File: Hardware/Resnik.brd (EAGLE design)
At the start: 64.8 x 100 mm, 213 parts, among them IC1 ATMEGA644M, J1 CONN_82.54_SCREW, J3 CONN_42.54_SCREW, J4 CONN_82.54_SCREW, Q1 DMG3404, Q2 DMG3404, Q3 FDN360P, Q4 2N7002, Q5 FDN360P, Q6 DMG3404, Q7 2N7002, Q8 2N7002, U1 TLV61220DBV, U10 TPS22917DBV, U11 SN74AUP1G04YFP, U12 SN74AUP1G04YFP, U13 SN74AUP1G04YFP, U14 SN74AUP2G08DQE, U15 SN74AUP2G08DQE, U16 SN74AUP2G08DQE, U17 MIC2544MSOP, U18 MIC2544MSOP, U19 MIC2544MSOP, U2 TPS62822DLC, U20 MIC2544MSOP, U21 TPS22917DBV, U22 TPS22917DBV, U23 FT231X-Q, U24 SN74LVC1G3157DRL, U25 SN74AUP3G34DCU, U26 TXS0102DQM, U27 TXS0104RGY, U28 TCA9406DCU, U29 TXS0104RGY, U3 TPS61032RSA, U30 MCP4726A2SOT-23, U31 BME280, U32 ADS1115, U33 ADS1115, U34 INA211DCK, U35 INA210DCK, U36 TCA9406DCU, U37 TLV3691DCK, U38 TS5A21366RSE, U39 MIC94090C6, U40 SN74AHC1G86DCK, U41 MCP23018QFN, U42 TXS0104RGY, U5 BQ2980RUG, U6 TPS2105, U7 LTC4412S6, U8 TPL5111DDC, U9 TPS79733

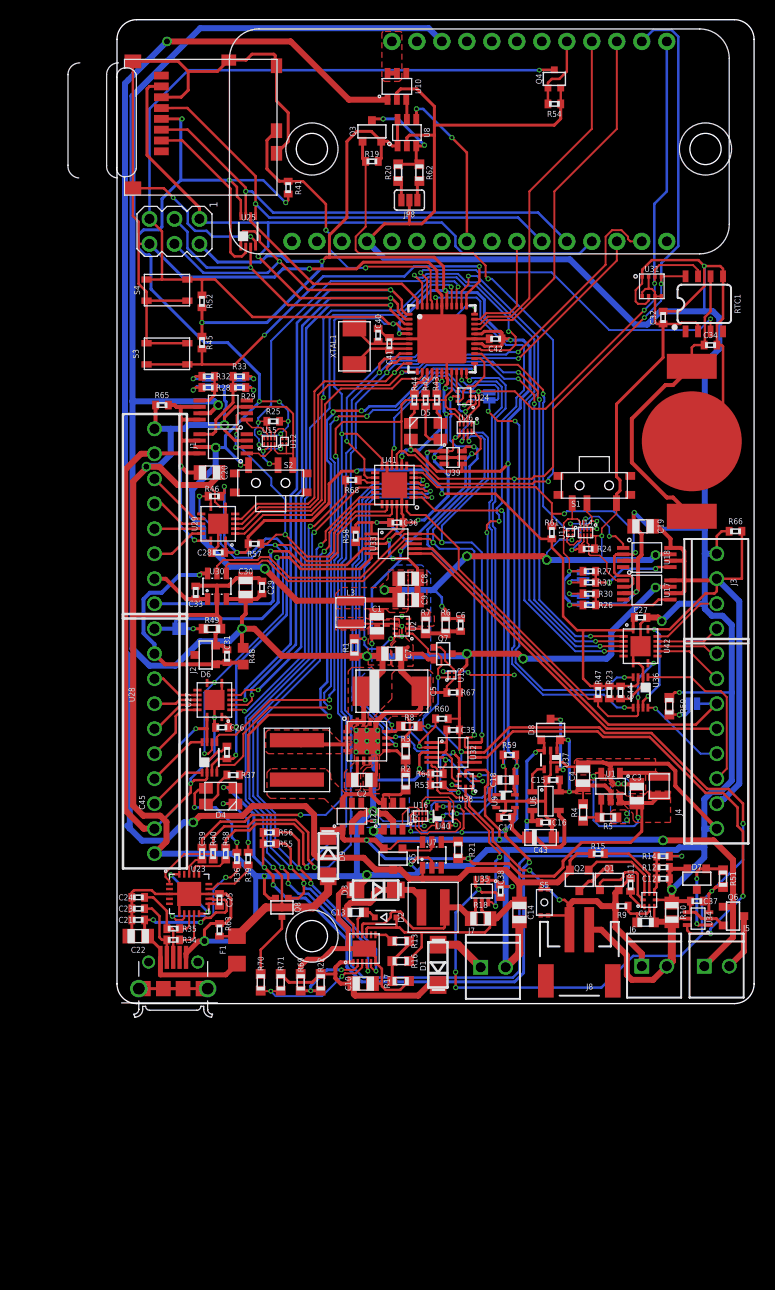
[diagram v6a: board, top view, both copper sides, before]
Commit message: Minor value changes, generated BoM for quote generation
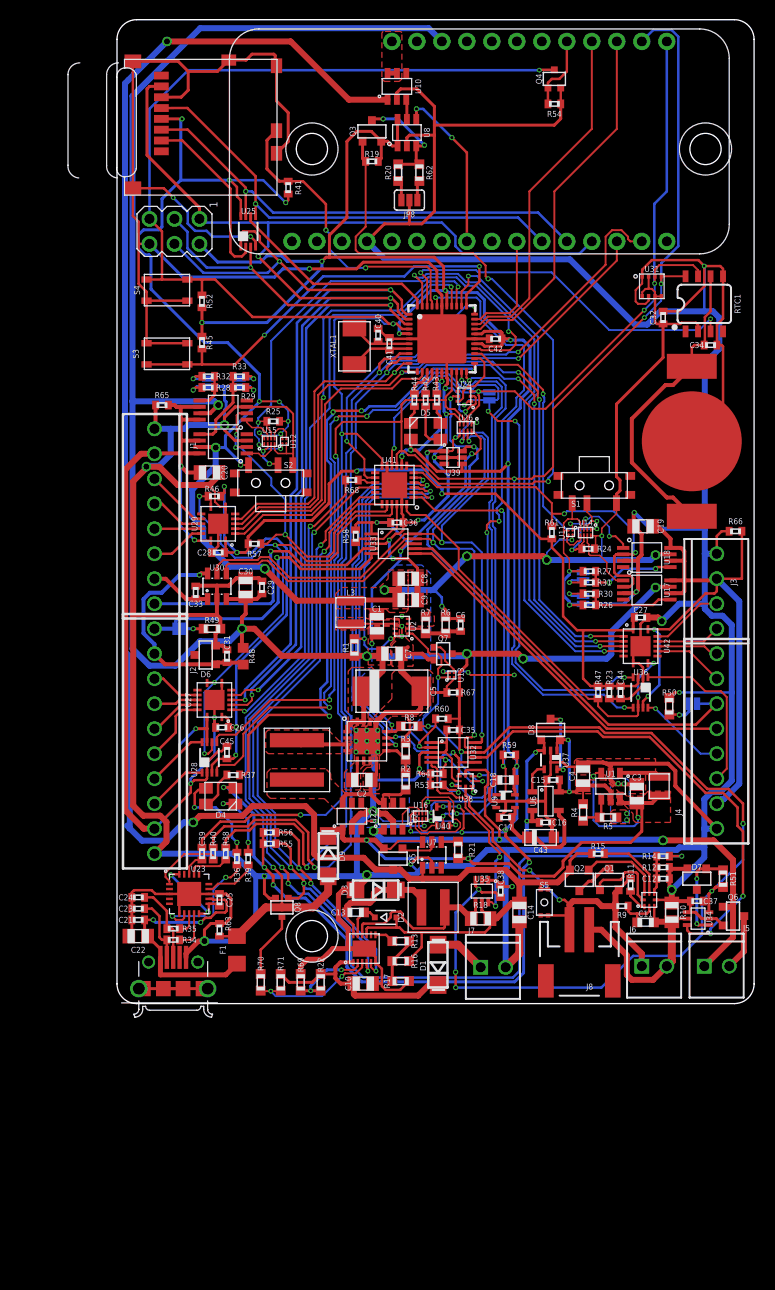
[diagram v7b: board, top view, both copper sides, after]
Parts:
- IC1: value ATMEGA644M -> ATMEGA1284M
- U35: value INA210DCK -> INA213DCK
- U39: value MIC94090C6 -> MIC94094C6

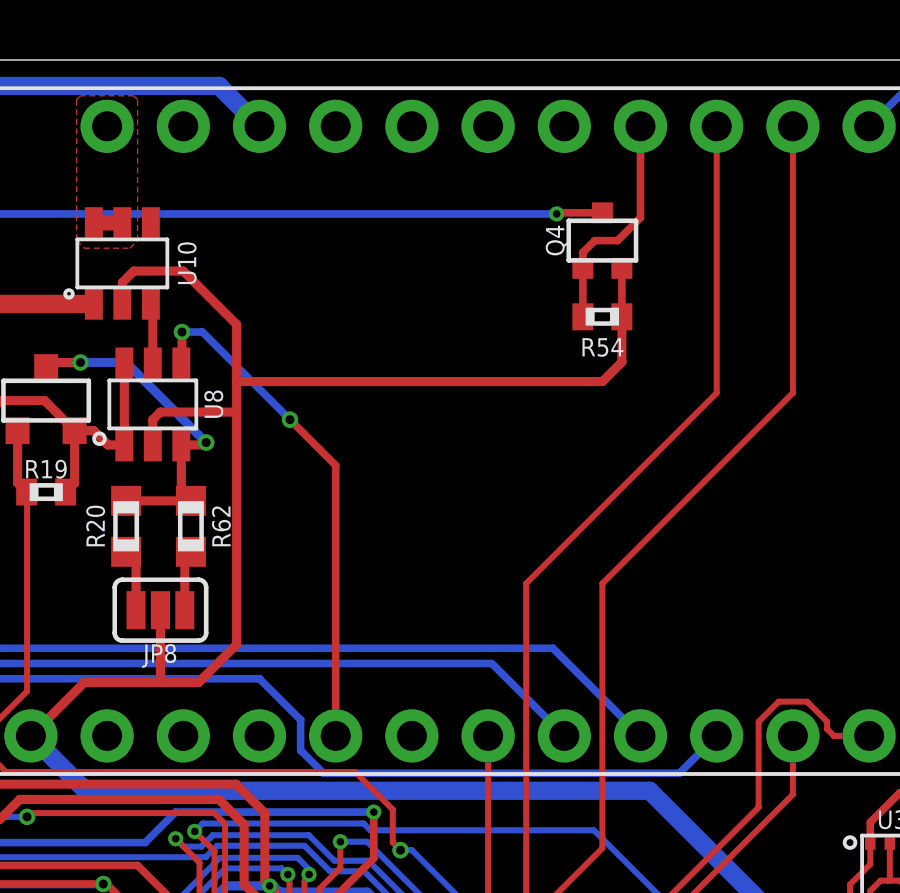
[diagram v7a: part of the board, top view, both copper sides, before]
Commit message: Added Ref ID images, updated BoM for new parts, added pick and place
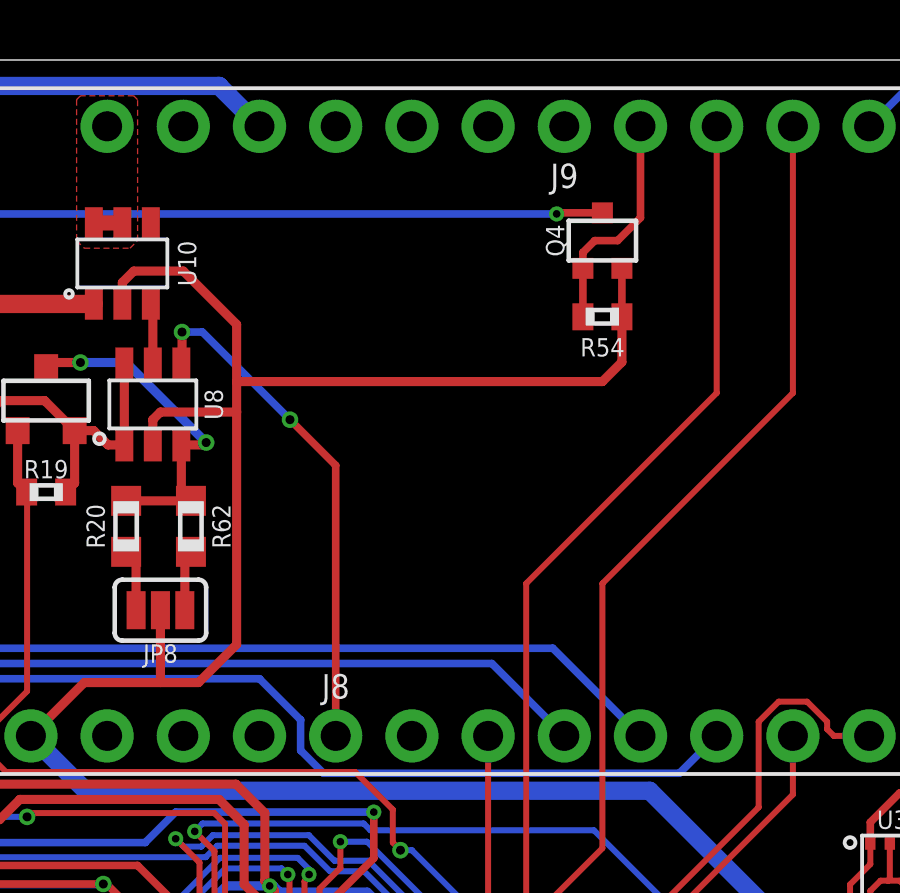
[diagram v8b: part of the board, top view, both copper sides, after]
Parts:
- C18: value 1uF -> 4.7uF
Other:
- board text added: "J8"
- board text added: "J9"
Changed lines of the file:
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@@
 <?xml version="1.0" encoding="utf-8"?>
 <!DOCTYPE eagle SYSTEM "eagle.dtd">
-<eagle version="9.2.1">
+<eagle version="9.4.2">
 <drawing>
 <settings>
@@
 <grid distance="50" unitdist="mil" unit="mm" style="lines" multiple="1" display="no" altdistance="5" altunitdist="mil" altunit="mm"/>
 <layers>
-<layer number="1" name="Top" color="4" fill="1" visible="no" active="yes"/>
+<layer number="1" name="Top" color="4" fill="1" visible="yes" active="yes"/>
 <layer number="2" name="Route2" color="16" fill="1" visible="no" active="no"/>
 <layer number="3" name="Route3" color="17" fill="1" visible="no" active="no"/>
@@
 <layer number="14" name="Route14" color="22" fill="1" visible="no" active="no"/>
 <layer number="15" name="Route15" color="23" fill="1" visible="no" active="no"/>
-<layer number="16" name="Bottom" color="1" fill="1" visible="no" active="yes"/>
+<layer number="16" name="Bottom" color="1" fill="1" visible="yes" active="yes"/>
 <layer number="17" name="Pads" color="2" fill="1" visible="yes" active="yes"/>
 <layer number="18" name="Vias" color="2" fill="1" visible="yes" active="yes"/>
@@
 <layer number="20" name="Dimension" color="24" fill="1" visible="yes" active="yes"/>
 <layer number="21" name="tPlace" color="7" fill="1" visible="yes" active="yes"/>
-<layer number="22" name="bPlace" color="7" fill="1" visible="yes" active="yes"/>
+<layer number="22" name="bPlace" color="7" fill="1" visible="no" active="yes"/>
 <layer number="23" name="tOrigins" color="15" fill="1" visible="yes" active="yes"/>
 <layer number="24" name="bOrigins" color="15" fill="1" visible="no" active="yes"/>
@@
 <dimension x1="19.812" y1="86.858" x2="19.812" y2="6.858" x3="-8.89" y3="46.858" textsize="0.8128" textratio="15" layer="48" dtype="vertical"/>
 <text x="27.432" y="81.661" size="0.8128" layer="51" font="vector" ratio="15" align="center">J6</text>
+<text x="35.56" y="79.121" size="0.8128" layer="25" font="vector" ratio="15" align="center">J8</text>
+<text x="43.18" y="96.139" size="0.8128" layer="25" font="vector" ratio="15" align="center">J9</text>
 </plain>
 <attributes>
@@
 </element>
 <element name="C11" library="bschulz_passives" package="C0603" value="1uF" x="53.721" y="8.255" smashed="yes">
-<attribute name="DIGIKEY" value="490-10479-1-ND" x="53.721" y="8.255" size="0.8128" layer="27" font="vector" ratio="15" display="off"/>
-<attribute name="MF" value="Murata" x="53.721" y="8.255" size="0.8128" layer="27" font="vector" ratio="15" display="off"/>
-<attribute name="MPN" value="GRM188R61C105KA12D" x="53.721" y="8.255" size="0.8128" layer="27" font="vector" ratio="15" display="off"/>
+<attribute name="DIGIKEY" value="587-1251-1-ND" x="53.721" y="8.255" size="0.8128" layer="27" font="vector" ratio="15" display="off"/>
+<attribute name="MF" value="Yaiyo Yuden" x="53.721" y="8.255" size="0.8128" layer="27" font="vector" ratio="15" display="off"/>
+<attribute name="MPN" value="EMK107BJ105KA-T" x="53.721" y="8.255" size="0.8128" layer="27" font="vector" ratio="15" display="off"/>
 <attribute name="NAME" x="53.721" y="9.144" size="0.6096" layer="25" font="vector" ratio="15" align="center"/>
 <attribute name="VALUE" x="53.721" y="6.858" size="0.6096" layer="27" font="vector" ratio="15" align="center"/>
@@
 </element>
 <element name="C13" library="bschulz_passives" package="C0603" value="1uF" x="24.257" y="9.271" smashed="yes">
-<attribute name="DIGIKEY" value="490-10479-1-ND" x="24.257" y="9.271" size="0.8128" layer="27" font="vector" ratio="15" display="off"/>
-<attribute name="MF" value="Murata" x="24.257" y="9.271" size="0.8128" layer="27" font="vector" ratio="15" display="off"/>
-<attribute name="MPN" value="GRM188R61C105KA12D" x="24.257" y="9.271" size="0.8128" layer="27" font="vector" ratio="15" display="off"/>
+<attribute name="DIGIKEY" value="587-1251-1-ND" x="24.257" y="9.271" size="0.8128" layer="27" font="vector" ratio="15" display="off"/>
+<attribute name="MF" value="Yaiyo Yuden" x="24.257" y="9.271" size="0.8128" layer="27" font="vector" ratio="15" display="off"/>
+<attribute name="MPN" value="EMK107BJ105KA-T" x="24.257" y="9.271" size="0.8128" layer="27" font="vector" ratio="15" display="off"/>
 <attribute name="NAME" x="22.479" y="9.271" size="0.6096" layer="25" font="vector" ratio="15" align="center"/>
 <attribute name="VALUE" x="24.257" y="7.874" size="0.6096" layer="27" font="vector" ratio="15" align="center"/>
@@
 <attribute name="VALUE" x="39.497" y="19.939" size="0.6096" layer="27" font="vector" ratio="15" rot="R180" align="center"/>
 </element>
-<element name="C18" library="bschulz_passives" package="C0603" value="1uF" x="39.497" y="22.733" smashed="yes" rot="R180">
-<attribute name="DIGIKEY" value="490-10479-1-ND" x="49.657" y="21.463" size="0.8128" layer="27" font="vector" ratio="15" rot="R180" display="off"/>
+<element name="C18" library="bschulz_passives" package="C0603" value="4.7uF" x="39.497" y="22.733" smashed="yes" rot="R180">
+<attribute name="DIGIKEY" value="490-10481-1-ND" x="49.657" y="21.463" size="0.8128" layer="27" font="vector" ratio="15" rot="R180" display="off"/>
 <attribute name="MF" value="Murata" x="49.657" y="21.463" size="0.8128" layer="27" font="vector" ratio="15" rot="R180" display="off"/>
-<attribute name="MPN" value="GRM188R61C105KA12D" x="49.657" y="21.463" size="0.8128" layer="27" font="vector" ratio="15" rot="R180" display="off"/>
+<attribute name="MPN" value="GRM188R61C475KAAJD" x="49.657" y="21.463" size="0.8128" layer="27" font="vector" ratio="15" rot="R180" display="off"/>
 <attribute name="NAME" x="38.227" y="22.733" size="0.6096" layer="25" font="vector" ratio="15" rot="R270" align="center"/>
 <attribute name="VALUE" x="39.497" y="24.13" size="0.6096" layer="27" font="vector" ratio="15" rot="R180" align="center"/>
